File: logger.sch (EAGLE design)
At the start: 78 parts, among them IC1 LTC4412, J1 POWER_JACKPTH, Q1 FDN360P, Q2 FDN360P, Q3 2N7002PW, Q4 2N7002PW, U1 DS3231MZ/V+T, U2 FT231X-Q

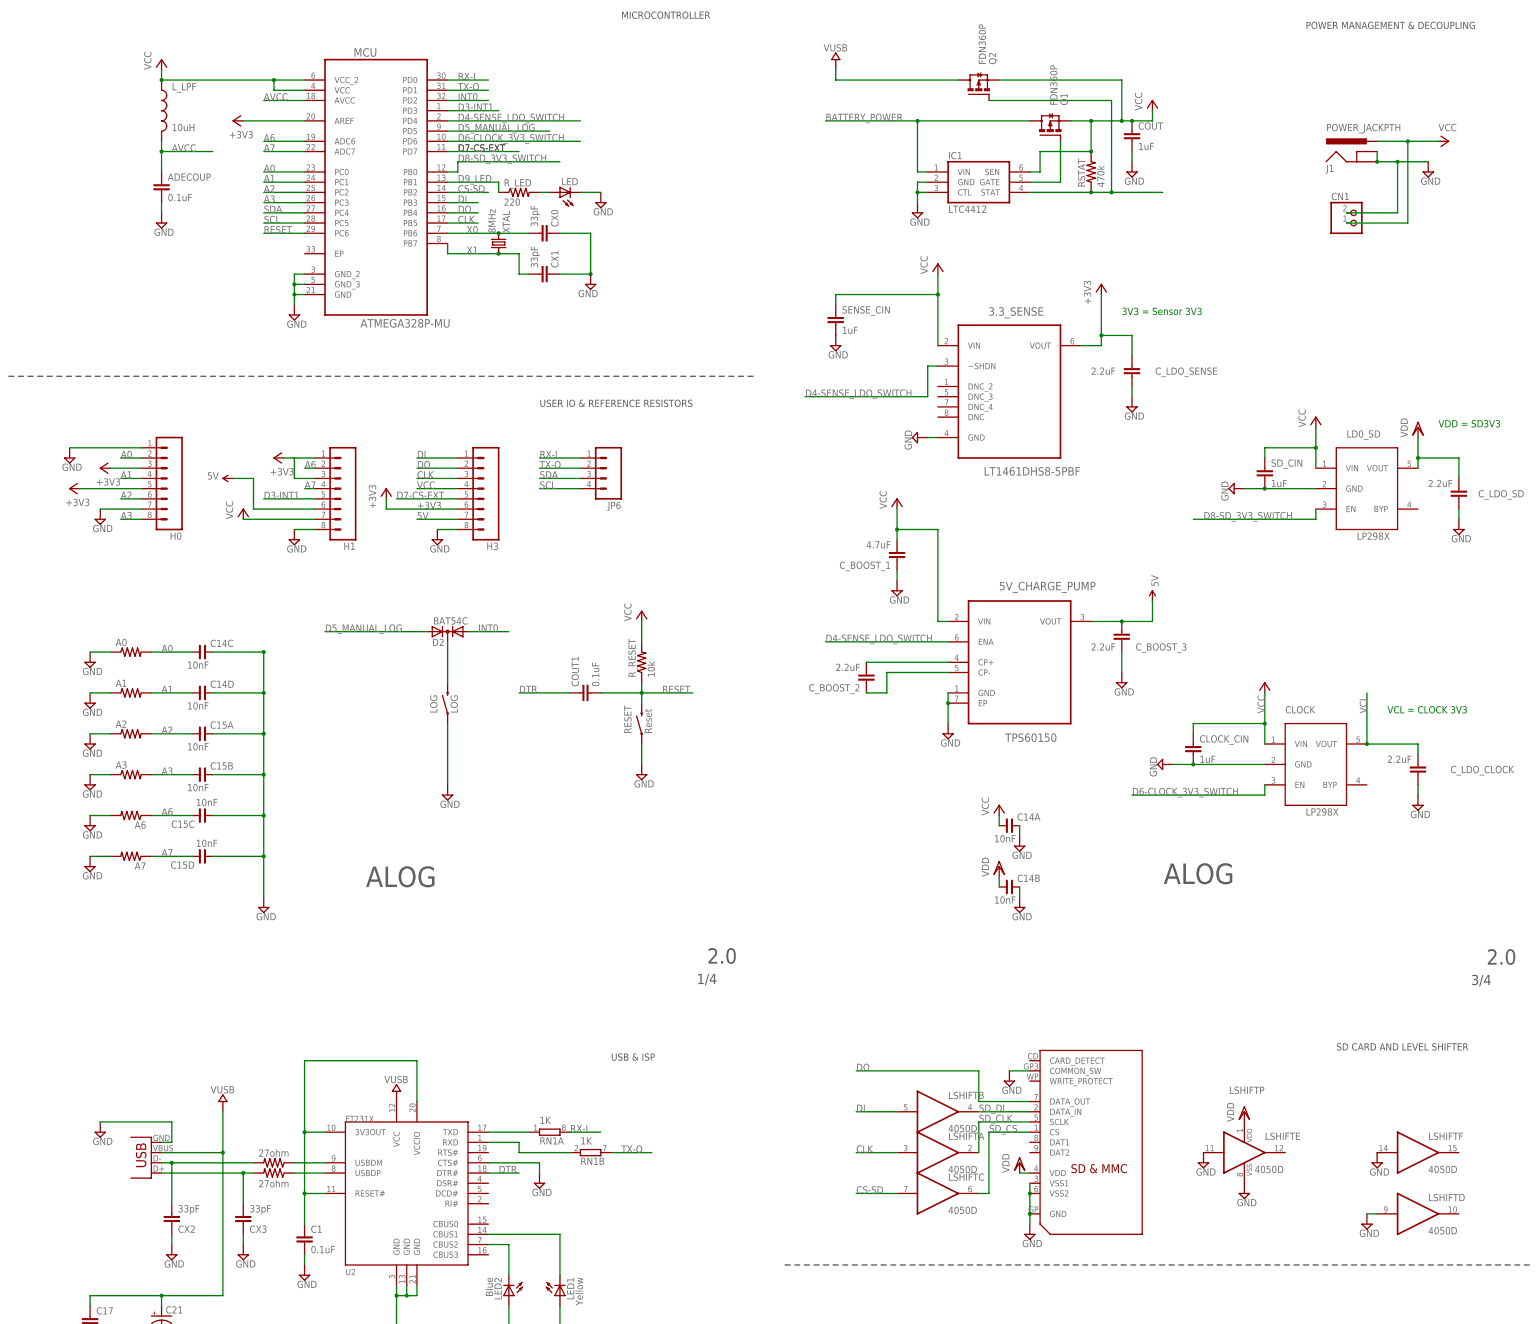
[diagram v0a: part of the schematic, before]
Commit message: change 3V3 power supply with jumpers, routing needs finishing
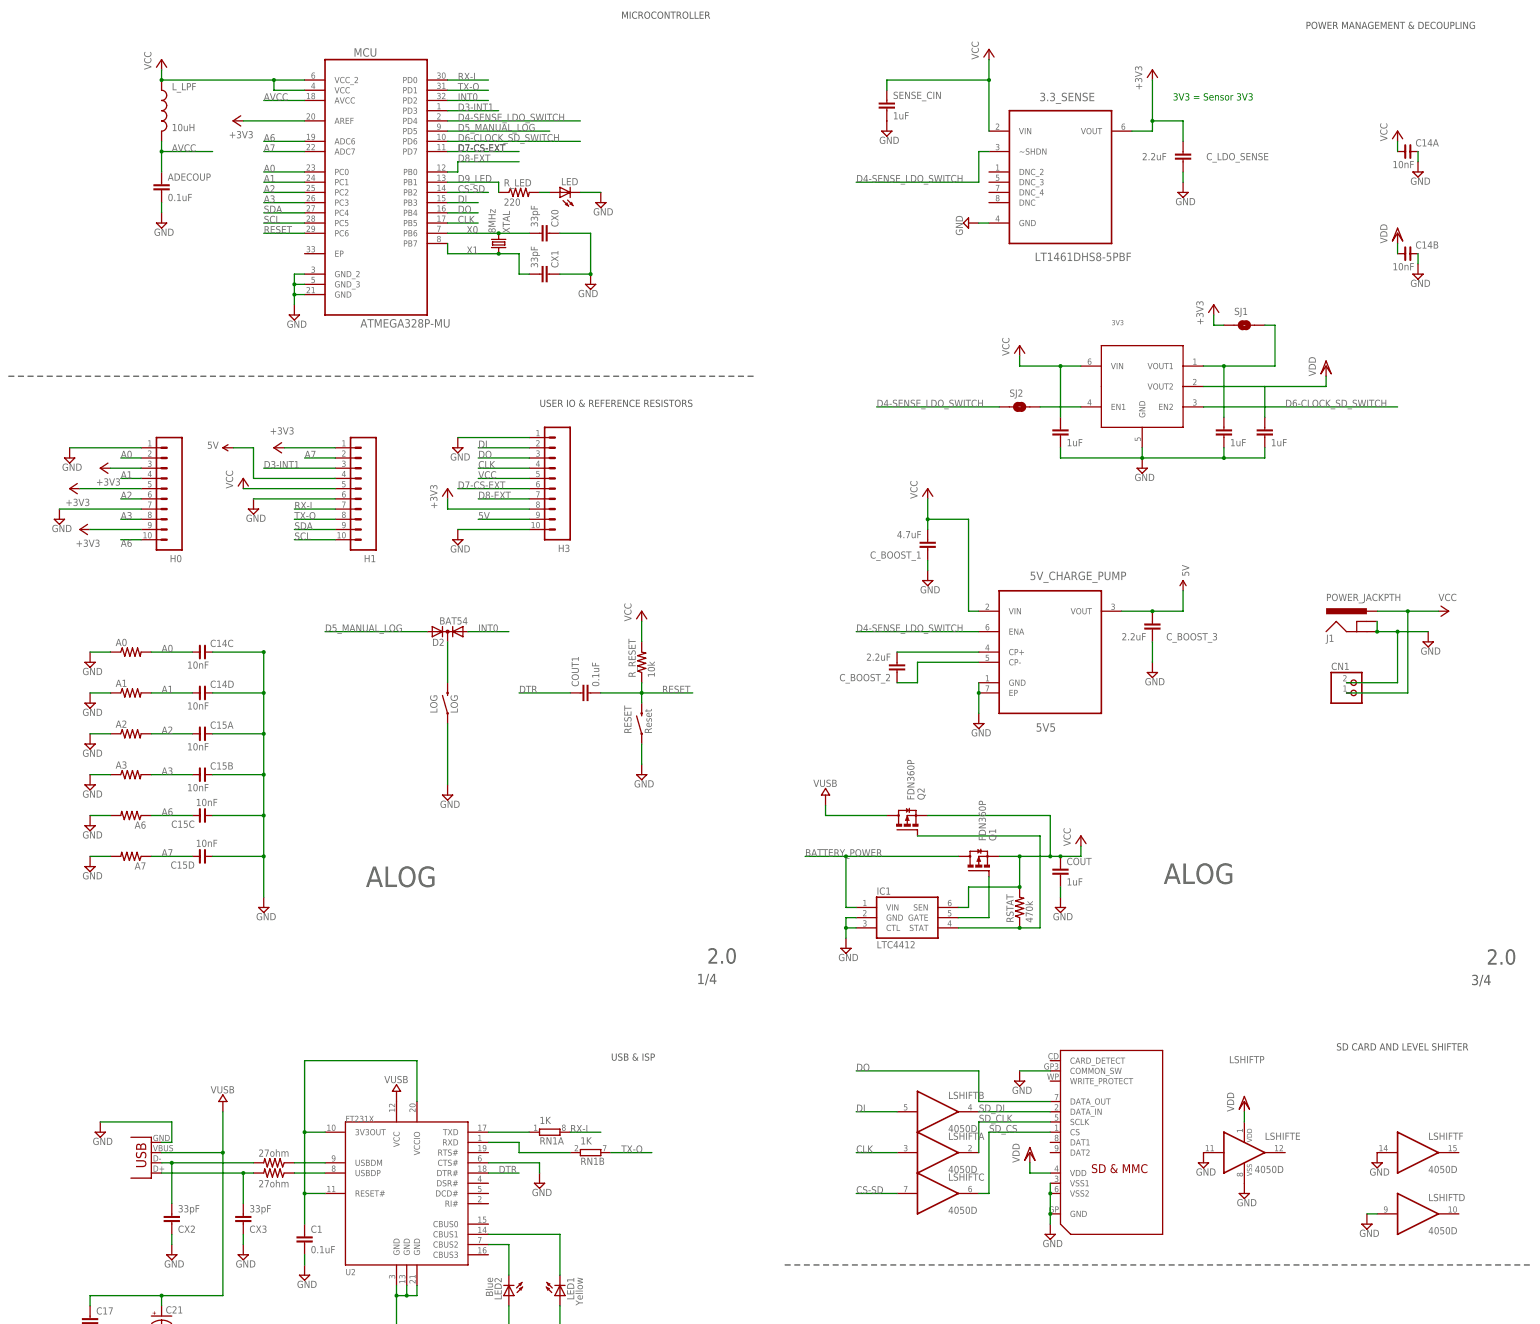
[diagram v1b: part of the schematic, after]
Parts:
- removed CLOCK, LD0_SD: LP2985, adafruit:LP298XS
- removed CLOCK_CIN, SD_CIN: 1uF, rcl:C-EUC0603
- removed C_LDO_CLOCK, C_LDO_SD: 2.2uF, resistor:C-EUC0603
- removed JP6: (no value), SparkFun-Connectors:M04SCREW
- added 3V3: (no value), csandell:MIC5380
- added CLOCK_CIN1, CLOCK_CIN2, CLOCK_CIN3: 1uF, rcl:C-EUC0603
- added SJ1, SJ2: SOLDERJUMPERNO, SparkFun-Retired:SOLDERJUMPERNO
- 5V_CHARGE_PUMP: value TPS60150 -> 5V5
- D2: value BAT54C -> BAT54
- H0, H1, H3: device SparkFun:M083.5MM-8 -> SparkFun-Connectors:M10-3.5MM
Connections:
- removed net D6-CLOCK_3V3_SWITCH: CLOCK.EN, MCU.PD6
- removed net D8-SD_3V3_SWITCH: LD0_SD.EN, MCU.PB0
- new net D6-CLOCK_SD_SWITCH: 3V3.EN2, MCU.PD6
- new net D8-EXT: H3.7, MCU.PB0
- new net N$19: 3V3.EN1, SJ2.2
- new net N$20: 3V3.VOUT1, CLOCK_CIN2.1, SJ1.2
- net +3V3: now also H0.9, H3.8, SJ1.1; no longer H1.3, H3.6
- net 5V: now also H1.4, H3.9; no longer H1.6, H3.7
- net A6: now also H0.10; no longer H1.2
- net A7: now also H1.2; no longer H1.4
- net CLK: now also H3.4; no longer H3.3
- net D3-INT1: now also H1.3; no longer H1.5
- net D4-SENSE_LDO_SWITCH: now also SJ2.1
- net D7-CS-EXT: now also H3.6; no longer H3.5
- net DI: now also H3.2; no longer H3.1
- net DO: now also H3.3; no longer H3.2
- net GND: now also 3V3.GND, CLOCK_CIN1.2, CLOCK_CIN2.2, CLOCK_CIN3.2, H1.6, H3.1, H3.10; no longer CLOCK.GND, CLOCK_CIN.2, C_LDO_CLOCK.1, C_LDO_SD.1, H1.8, H3.8, LD0_SD.GND, SD_CIN.2
- net RX-I: now also H1.7; no longer JP6.1
- net SCL: now also H1.10; no longer JP6.4
- net SDA: now also H1.9; no longer JP6.3
- net TX-O: now also H1.8; no longer JP6.2
- net VCC: now also 3V3.VIN, CLOCK_CIN1.1, H1.5, H3.5; no longer CLOCK.VIN, CLOCK_CIN.1, H1.7, H3.4, LD0_SD.VIN, SD_CIN.1
- net VCL: no longer CLOCK.VOUT, C_LDO_CLOCK.2
- net VDD: now also 3V3.VOUT2, CLOCK_CIN3.1; no longer C_LDO_SD.2, LD0_SD.VOUT
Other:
- note removed: "VCL = CLOCK 3V3"
- note removed: "VDD = SD3V3"
- moved on the sheet: 3.3_SENSE, 5V_CHARGE_PUMP, C14A, C14B, CN1, COUT, C_BOOST_1, C_BOOST_2, C_BOOST_3, C_LDO_SENSE, IC1, J1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

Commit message: Routed and ready for Wickert check of approval
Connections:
- net GND: now also MCU.EP
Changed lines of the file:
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@@
 <?xml version="1.0" encoding="utf-8"?>
 <!DOCTYPE eagle SYSTEM "eagle.dtd">
-<eagle version="6.6.0">
+<eagle version="7.7.0">
 <drawing>
 <settings>
@@
 <junction x="401.32" y="142.24"/>
 <junction x="401.32" y="139.7"/>
-</segment>
-<segment>
+<pinref part="MCU" gate="A" pin="EP"/>
+<wire x1="403.86" y1="149.86" x2="401.32" y2="149.86" width="0.1524" layer="91"/>
+<wire x1="401.32" y1="149.86" x2="401.32" y2="144.78" width="0.1524" layer="91"/>
+<junction x="401.32" y="144.78"/>
+</segment>
+<segment>

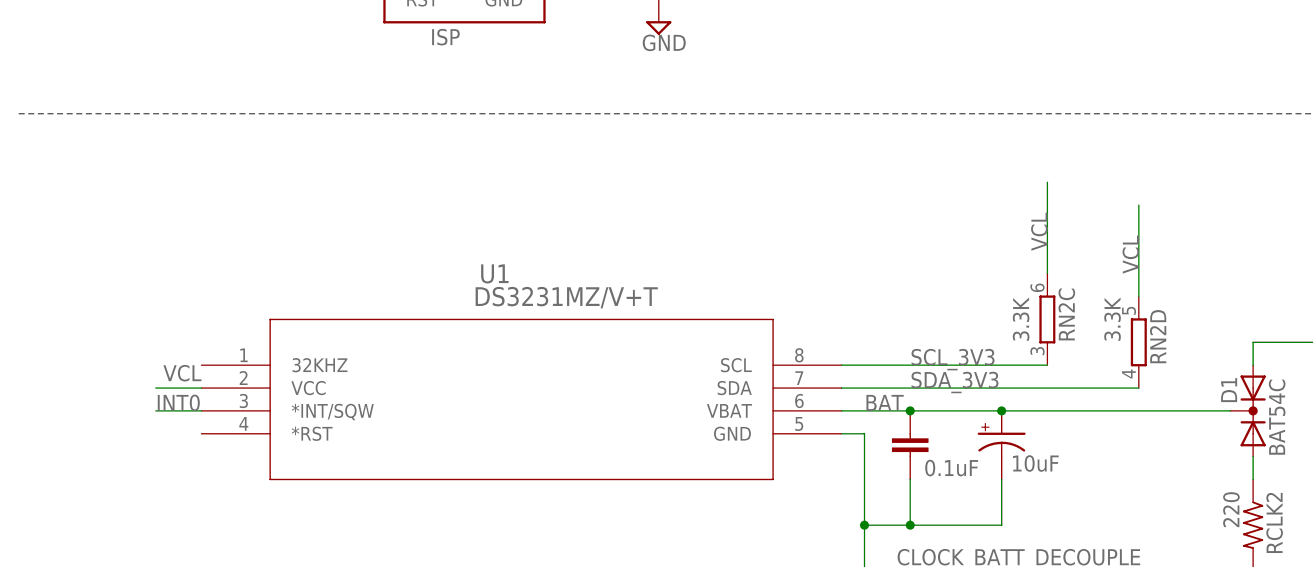
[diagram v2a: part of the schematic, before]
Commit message: Connected VDD to VCL
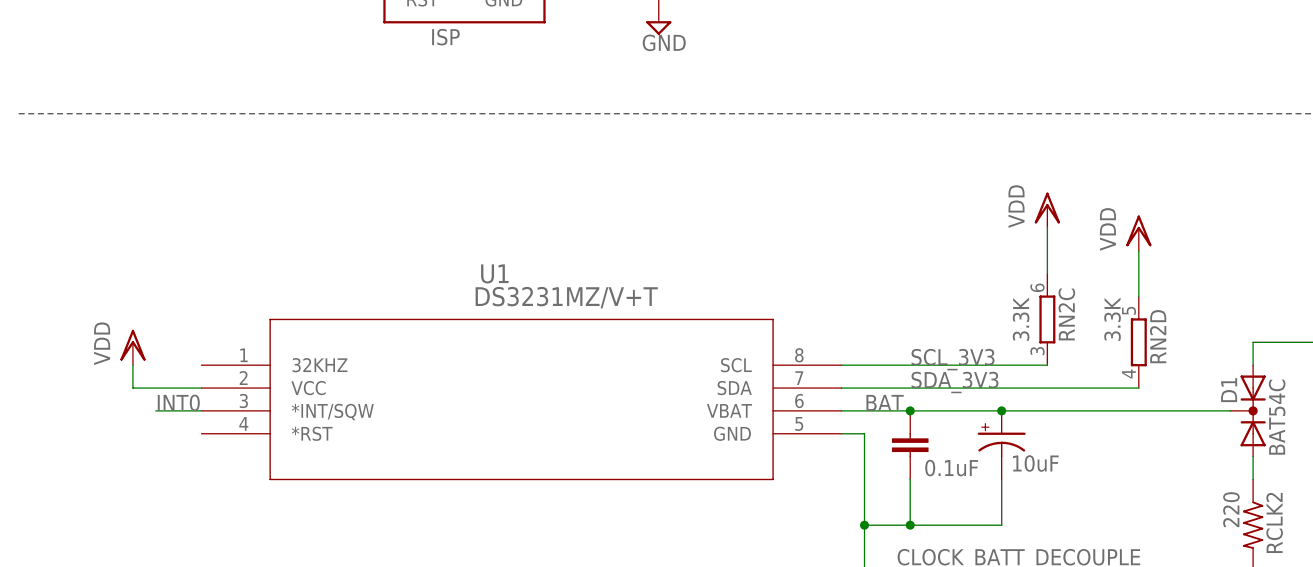
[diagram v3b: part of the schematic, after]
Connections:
- removed net VCL: RN2C.2, RN2D.2, U1.VCC
- net VDD: now also RN2C.2, RN2D.2, U1.VCC
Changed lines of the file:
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@@
 <part name="+3V7" library="supply1" deviceset="+3V3" device=""/>
 <part name="SUPPLY51" library="supply2" deviceset="GND" device=""/>
+<part name="SD_3V3" library="supply1" deviceset="VDD" device=""/>
+<part name="SD_3V5" library="supply1" deviceset="VDD" device=""/>
+<part name="SD_3V6" library="supply1" deviceset="VDD" device=""/>
 </parts>
 <sheets>
@@
 <instance part="+3V7" gate="G$1" x="347.98" y="81.28" rot="R90"/>
 <instance part="SUPPLY51" gate="GND" x="441.96" y="101.6"/>
+<instance part="SD_3V3" gate="G$1" x="454.66" y="-172.72"/>
+<instance part="SD_3V5" gate="G$1" x="444.5" y="-170.18"/>
+<instance part="SD_3V6" gate="G$1" x="342.9" y="-185.42"/>
 </instances>
 <busses>
@@
 <pinref part="SD_3V4" gate="G$1" pin="VDD"/>
 </segment>
+<segment>
+<wire x1="454.66" y1="-175.26" x2="454.66" y2="-180.34" width="0.1524" layer="91"/>
+<pinref part="RN2" gate="D" pin="2"/>
+<pinref part="SD_3V3" gate="G$1" pin="VDD"/>
+</segment>
+<segment>
+<wire x1="444.5" y1="-172.72" x2="444.5" y2="-177.8" width="0.1524" layer="91"/>
+<pinref part="RN2" gate="C" pin="2"/>
+<pinref part="SD_3V5" gate="G$1" pin="VDD"/>
+</segment>
+<segment>
+<wire x1="350.52" y1="-190.5" x2="342.9" y2="-190.5" width="0.1524" layer="91"/>
+<pinref part="U1" gate="A" pin="VCC"/>
+<wire x1="342.9" y1="-190.5" x2="342.9" y2="-187.96" width="0.1524" layer="91"/>
+<pinref part="SD_3V6" gate="G$1" pin="VDD"/>
+</segment>
 </net>
 <net name="LED+" class="0">
@@
 <pinref part="D2" gate="G$1" pin="K"/>
 <wire x1="439.42" y1="43.18" x2="439.42" y2="53.34" width="0.1524" layer="91"/>
-</segment>
-</net>
-<net name="VCL" class="0">
-<segment>
-<wire x1="350.52" y1="-190.5" x2="345.44" y2="-190.5" width="0.1524" layer="91"/>
-<label x="350.52" y="-187.96" size="1.778" layer="95" rot="R180"/>
-<pinref part="U1" gate="A" pin="VCC"/>
-</segment>
-<segment>
-<wire x1="444.5" y1="-167.64" x2="444.5" y2="-177.8" width="0.1524" layer="91"/>
-<pinref part="RN2" gate="C" pin="2"/>
-<label x="444.5" y="-175.26" size="1.778" layer="95" rot="R90"/>
-</segment>
-<segment>
-<wire x1="454.66" y1="-170.18" x2="454.66" y2="-180.34" width="0.1524" layer="91"/>
-<pinref part="RN2" gate="D" pin="2"/>
-<label x="454.66" y="-177.8" size="1.778" layer="95" rot="R90"/>
 </segment>
 </net>
@@
 </sheet>
 </sheets>
-<errors>
-</errors>
 </schematic>
 </drawing>

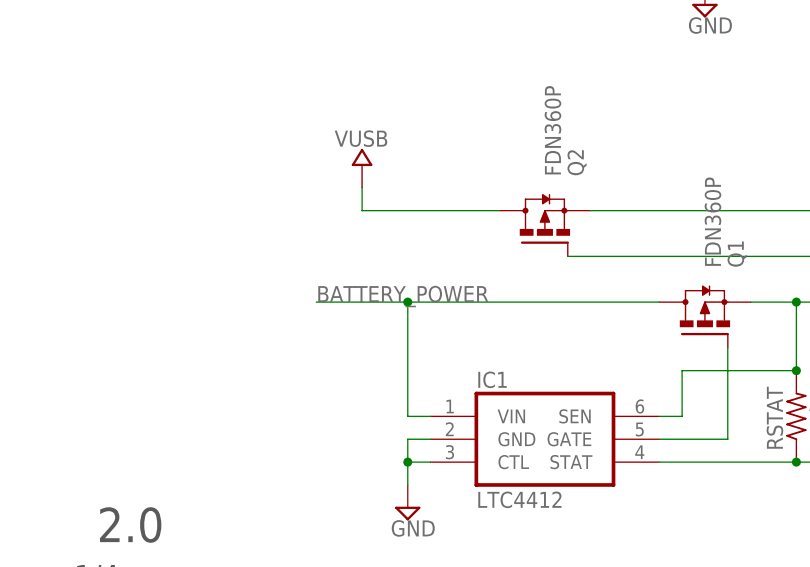
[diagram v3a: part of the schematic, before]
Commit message: 4412 routing fix and silkscreen gerber fix
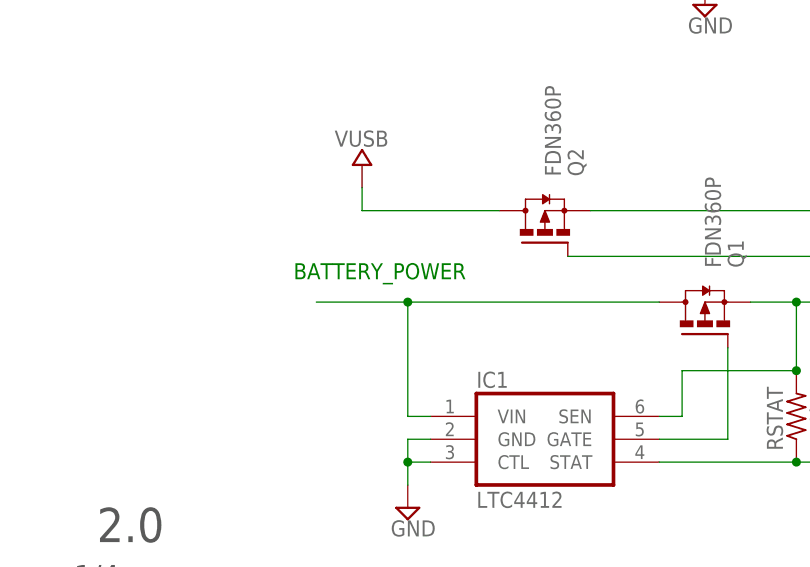
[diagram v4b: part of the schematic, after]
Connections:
- removed net BATTERY_POWER: IC1.VIN, Q1.D
- net VCC: now also IC1.VIN, Q1.D
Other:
- note added: "BATTERY_POWER"
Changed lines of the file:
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@@
 <?xml version="1.0" encoding="utf-8"?>
 <!DOCTYPE eagle SYSTEM "eagle.dtd">
-<eagle version="7.7.0">
+<eagle version="6.6.0">
 <drawing>
 <settings>
@@
 <text x="693.928" y="-32.004" size="2.54" layer="97">3/4</text>
 <text x="693.928" y="-288.29" size="2.54" layer="97">4/4</text>
+<text x="525.78" y="2.54" size="1.778" layer="91">BATTERY_POWER</text>
 </plain>
 <instances>
@@
 <wire x1="581.66" y1="121.92" x2="581.66" y2="124.46" width="0.1524" layer="91"/>
 </segment>
+<segment>
+<wire x1="541.02" y1="-12.7" x2="538.48" y2="-12.7" width="0.1524" layer="91"/>
+<wire x1="538.48" y1="-12.7" x2="538.48" y2="0" width="0.1524" layer="91"/>
+<pinref part="Q1" gate="G$1" pin="D"/>
+<wire x1="538.48" y1="0" x2="566.42" y2="0" width="0.1524" layer="91"/>
+<wire x1="538.48" y1="0" x2="528.32" y2="0" width="0.1524" layer="91"/>
+<junction x="538.48" y="0"/>
+<pinref part="IC1" gate="G$1" pin="VIN"/>
+</segment>
 </net>
 <net name="CS-SD" class="0">
@@
 </segment>
 </net>
-<net name="BATTERY_POWER" class="0">
-<segment>
-<wire x1="541.02" y1="-12.7" x2="538.48" y2="-12.7" width="0.1524" layer="91"/>
-<wire x1="538.48" y1="-12.7" x2="538.48" y2="0" width="0.1524" layer="91"/>
-<pinref part="Q1" gate="G$1" pin="D"/>
-<wire x1="538.48" y1="0" x2="566.42" y2="0" width="0.1524" layer="91"/>
-<wire x1="538.48" y1="0" x2="528.32" y2="0" width="0.1524" layer="91"/>
-<junction x="538.48" y="0"/>
-<label x="528.32" y="0" size="1.778" layer="95"/>
-<pinref part="IC1" gate="G$1" pin="VIN"/>
-</segment>
-</net>
